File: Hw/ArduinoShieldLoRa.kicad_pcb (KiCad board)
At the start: 2 copper layers, 57.6 x 53.3 mm, 27 parts, among them J1 DIO1, J2 DIO4, J3 CONN_01X01, J4 DIO3, J5 DIO5, J6 DIO2, P1 Power, P2 Analog, P3 Digital, P4 Digital, P5 CONN_01X01, P6 CONN_01X01, P7 CONN_01X01, P8 CONN_01X01, U1 RFM95, U2 74HC4050D, U3 AP2112K-3.3

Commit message: data place
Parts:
- moved svg2mod 0.25 mm to (150.0, 98.2)
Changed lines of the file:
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@@
   )
   (module Aesthetics:titule_electronic_med (layer B.Cu)
-    (at 150 98 180)
+    (at 150 98.25 180)
     (descr "Imported from ec.svg")
     (tags svg2mod)
@@
   (gr_line (start 176.8 123.8) (end 179.6 121) (layer Edge.Cuts) (width 0.15))
   (gr_line (start 176.8 125.8) (end 176.8 123.8) (layer Edge.Cuts) (width 0.15))
-  (gr_arc (start 145.3 116.9) (end 145.1 115) (angle 99.58534033) (layer F.SilkS) (width 0.15))
-  (gr_arc (start 145.3 116.8) (end 145.5 116.2) (angle 62.10272897) (layer F.SilkS) (width 0.15))
-  (gr_arc (start 145.4 116.8) (end 145.4 115.6) (angle 96.00900596) (layer F.SilkS) (width 0.15))
+  (gr_arc (start 145.8 115.15) (end 145.6 113.25) (angle 99.58534033) (layer F.SilkS) (width 0.15))
+  (gr_arc (start 145.8 115.05) (end 146 114.45) (angle 62.10272897) (layer F.SilkS) (width 0.15))
+  (gr_arc (start 145.9 115.05) (end 145.9 113.85) (angle 96.00900596) (layer F.SilkS) (width 0.15))
   (gr_line (start 122.428 114.3) (end 122.428 123.19) (angle 90) (layer Dwgs.User) (width 0.15))
   (gr_line (start 109.093 123.19) (end 109.093 114.3) (angle 90) (layer Dwgs.User) (width 0.15))
@@
   (gr_line (start 178.435 94.615) (end 178.435 102.235) (angle 90) (layer Dwgs.User) (width 0.15))
   (gr_line (start 173.355 102.235) (end 173.355 94.615) (angle 90) (layer Dwgs.User) (width 0.15))
-  (gr_text "CatWAN Shield" (at 137.5 117.7) (layer F.SilkS)
+  (gr_text "CatWAN Shield" (at 138 115.95) (layer F.SilkS)
     (effects (font (size 1.5 1.5) (thickness 0.3)))
   )
-  (gr_text "Node ID" (at 127.25 95.5) (layer F.SilkS)
+  (gr_text "Node ID" (at 127.25 91.5) (layer F.SilkS)
     (effects (font (size 1.5 1.5) (thickness 0.3)))
   )
-  (gr_text NOTES (at 126.25 105) (layer F.SilkS)
+  (gr_text NOTES (at 126.25 103) (layer F.SilkS)
     (effects (font (size 1.5 1.5) (thickness 0.3)))
   )
-  (gr_text 1 (at 136 124 90) (layer F.SilkS)
+  (gr_text 1 (at 136 124.25 90) (layer F.SilkS)
     (effects (font (size 1 1) (thickness 0.15)))
   )
-  (gr_text "Version 1.0" (at 136 120 360) (layer F.SilkS)
+  (gr_text "Version 1.0" (at 136.5 118.25 360) (layer F.SilkS)
     (effects (font (size 1.5 1.5) (thickness 0.3)))
   )
@@
     (polygon
       (pts
-        (xy 123 103) (xy 152 103) (xy 152 97) (xy 123 97)
+        (xy 123 99.25) (xy 152 99.25) (xy 152 93.25) (xy 123 93.25)
       )
     )
@@
     (polygon
       (pts
-        (xy 123 112) (xy 123 106) (xy 152 106) (xy 152 112)
+        (xy 123 110.5) (xy 123 104.5) (xy 152 104.5) (xy 152 110.5)
       )
     )

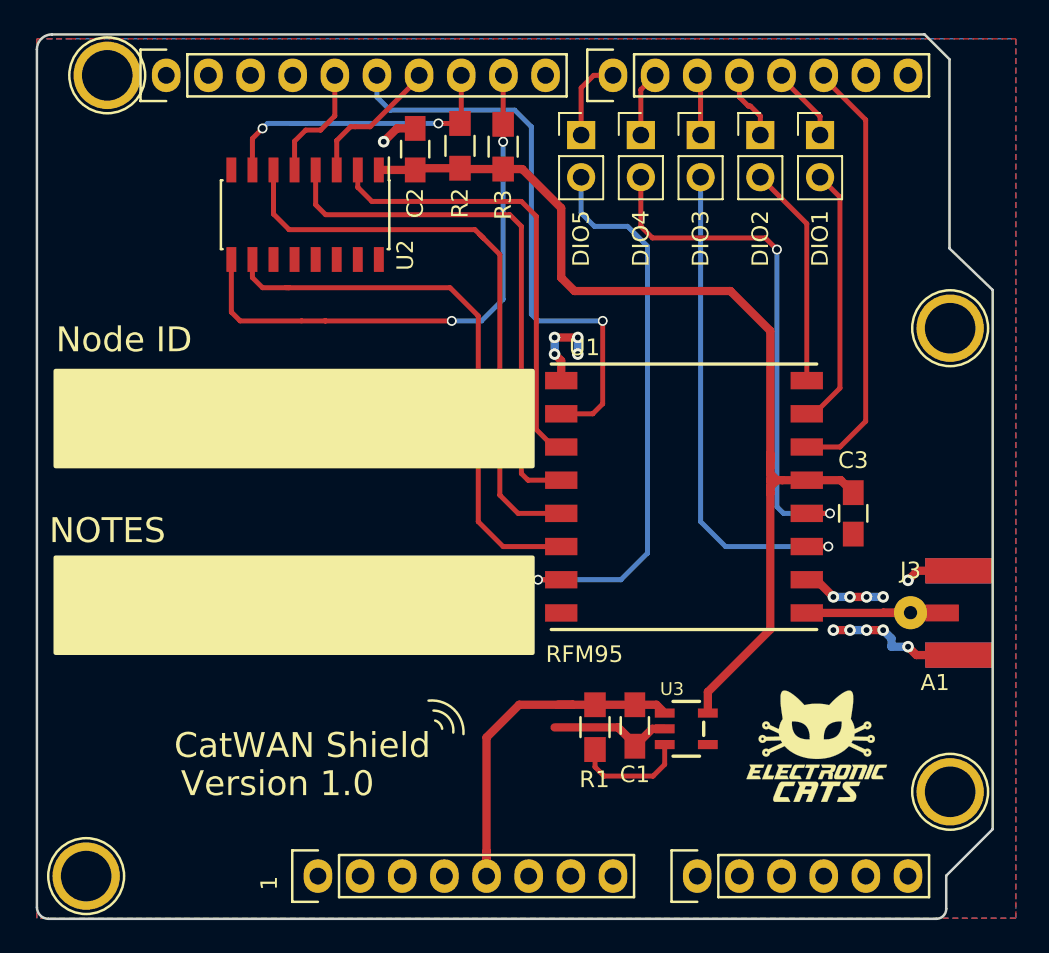
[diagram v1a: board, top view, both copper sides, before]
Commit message: Update to KiCad 6.0
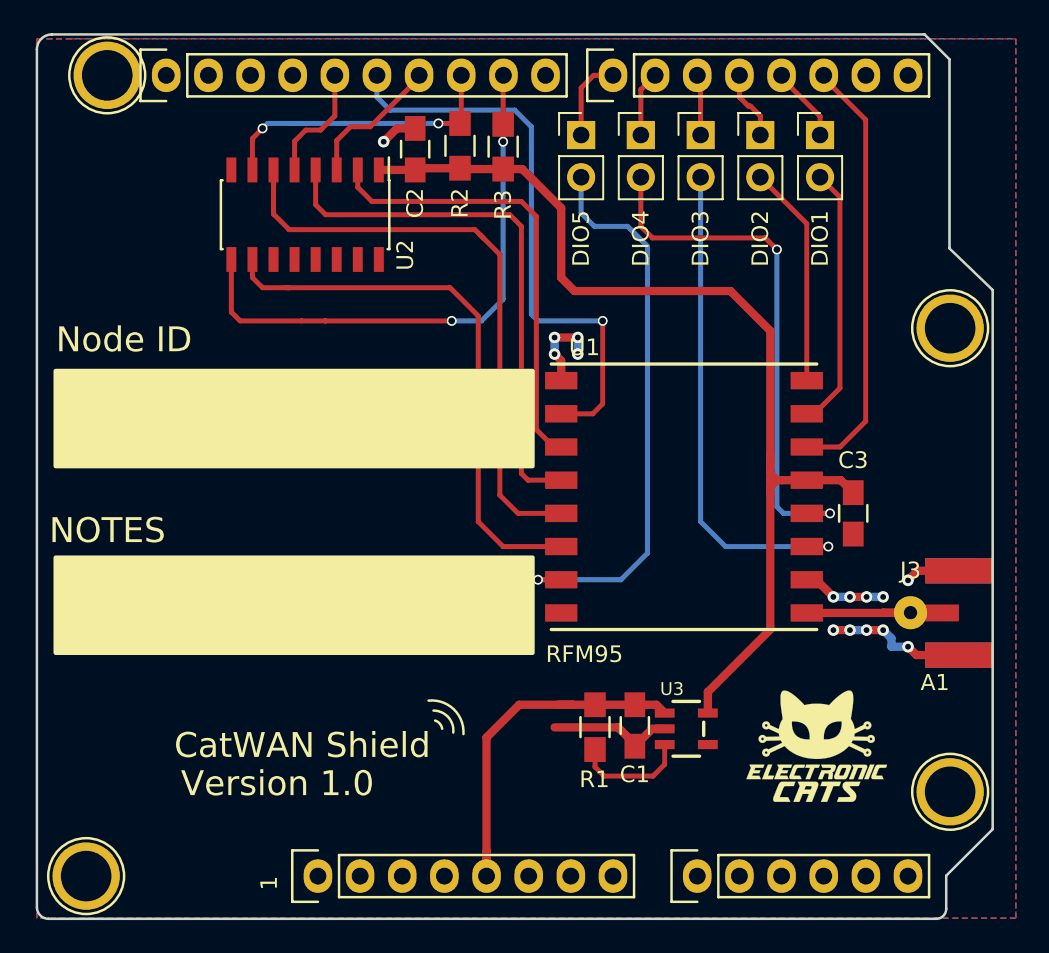
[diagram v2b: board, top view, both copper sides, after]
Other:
- net class Default removed
- net class Vcc removed
